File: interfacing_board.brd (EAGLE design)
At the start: 85.1 x 77.1 mm, 67 parts, among them IC1 MAX3096CSE, IC2 MAX3096CSE, X1 87758-3816, X2 87758-3816

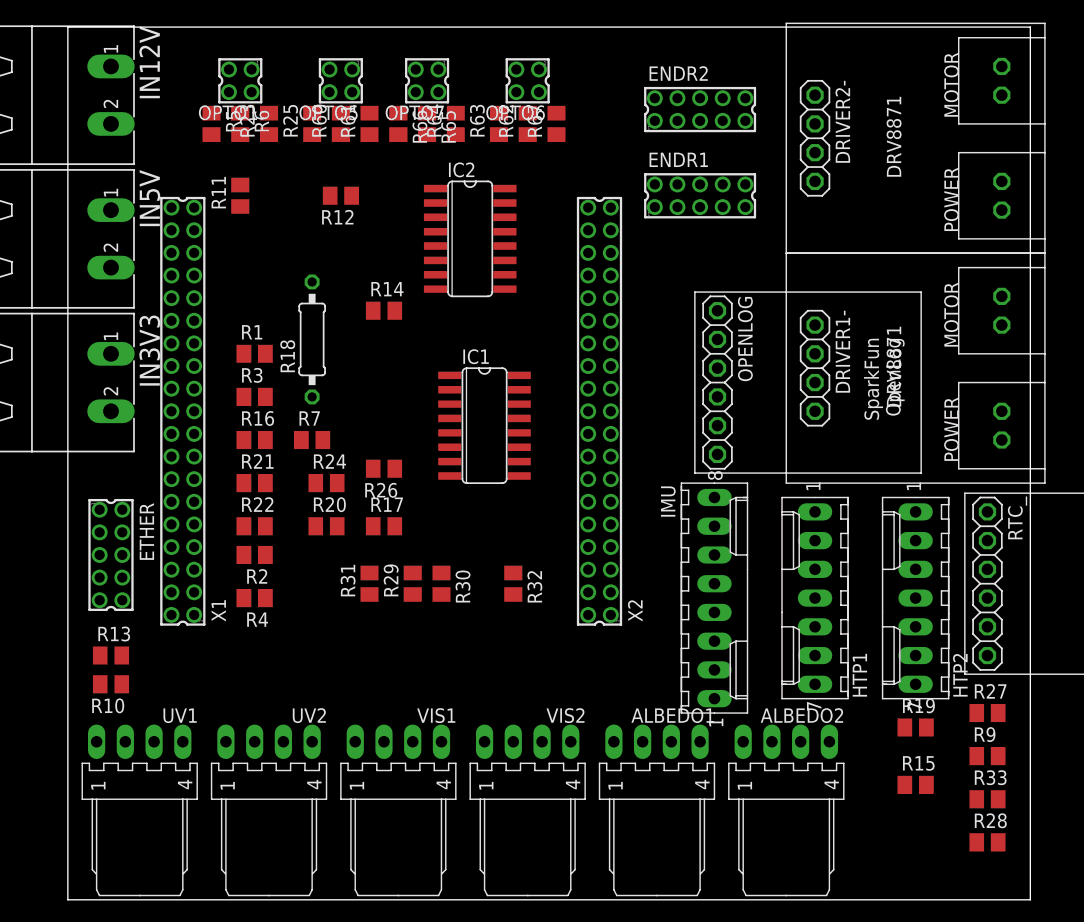
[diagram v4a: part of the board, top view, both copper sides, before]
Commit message: Autorouter on BIPOP board.
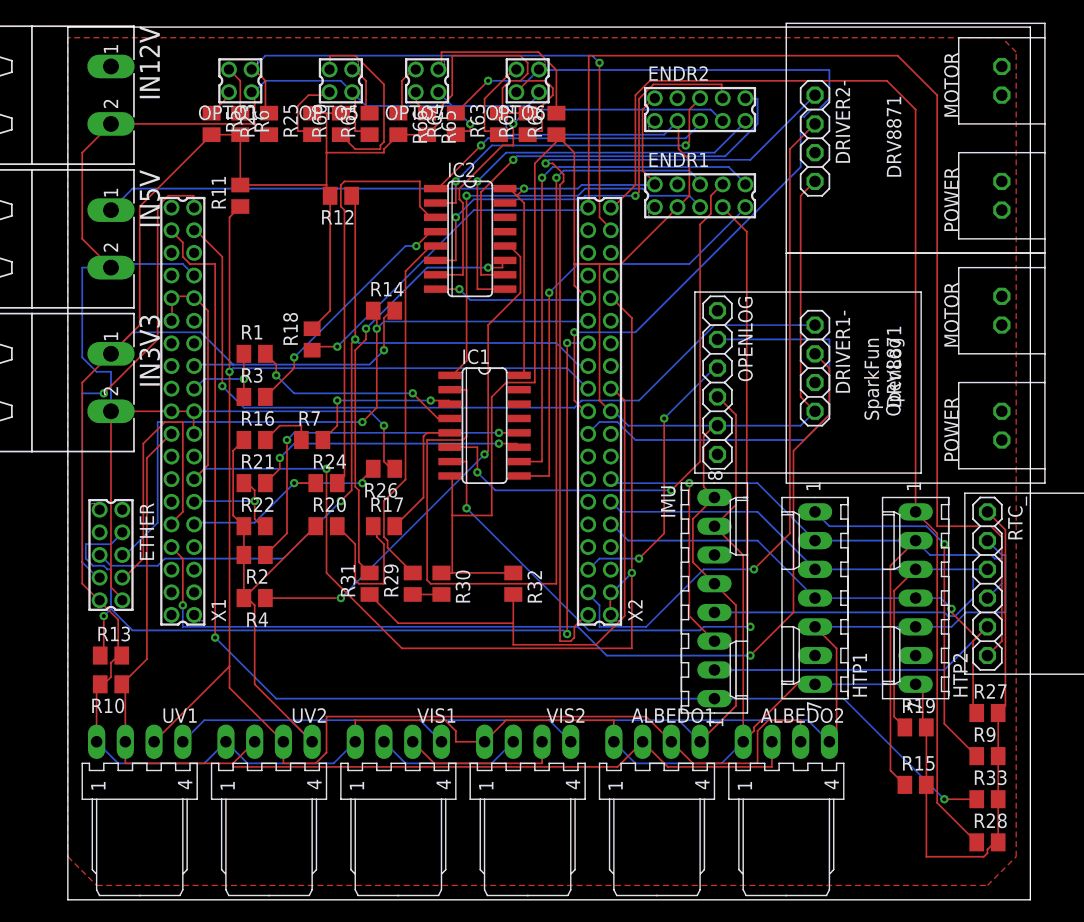
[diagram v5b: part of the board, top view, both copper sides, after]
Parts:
- R18: value 2k -> 4.7k; device eagle-ltspice:0207/10 -> rcl:R0805
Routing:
- net GND: track 0.00 -> 499.2 mm, vias 0 -> 3
- net 3.3V: track 0.00 -> 337.0 mm, vias 0 -> 1
- net SCL1: track 0.00 -> 149.7 mm, vias 0 -> 1
- net CS_RTC: track 0.00 -> 130.7 mm, vias 0 -> 1
- net CS_IMU: track 0.00 -> 112.1 mm, vias 0 -> 2
- net NC: track 0.00 -> 108.7 mm, vias 0 -> 2
- net CS_HTP2: track 0.00 -> 104.3 mm
- net SDA1: track 0.00 -> 95.3 mm
- net M11: track 0.00 -> 88.8 mm, vias 0 -> 2
- net SPI1_MISO: track 0.00 -> 84.6 mm, vias 0 -> 3
- net INCHA-1: track 0.00 -> 82.7 mm, vias 0 -> 1
- net SPI2_MOSI: track 0.00 -> 79.4 mm, vias 0 -> 1
- net IND2: track 0.00 -> 78.5 mm, vias 0 -> 2
- net SPI2_MISO: track 0.00 -> 77.1 mm
- net 5V: track 0.00 -> 76.1 mm, vias 0 -> 1
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- added copper zone on layer 1, net GND

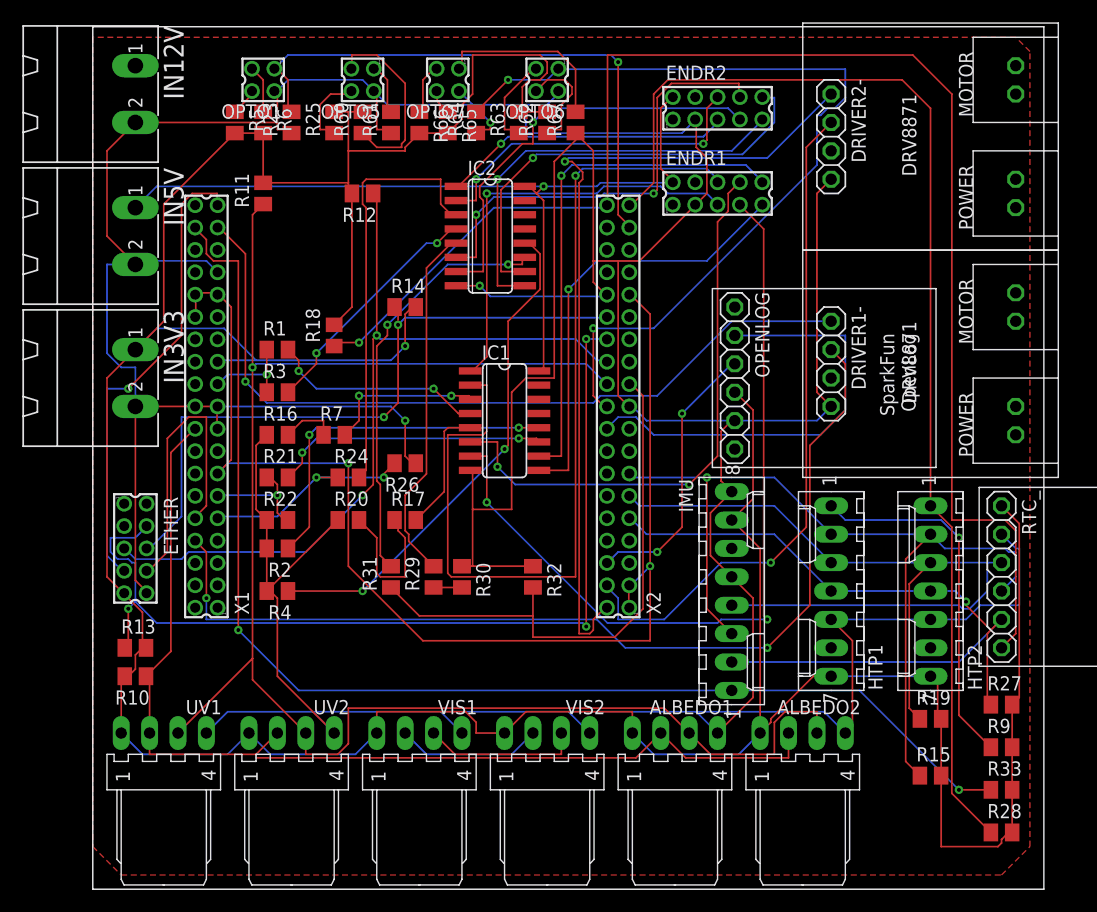
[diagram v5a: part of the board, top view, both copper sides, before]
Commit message: Changed connector in bipop_power_supply board, modified routing and board's dimensions.
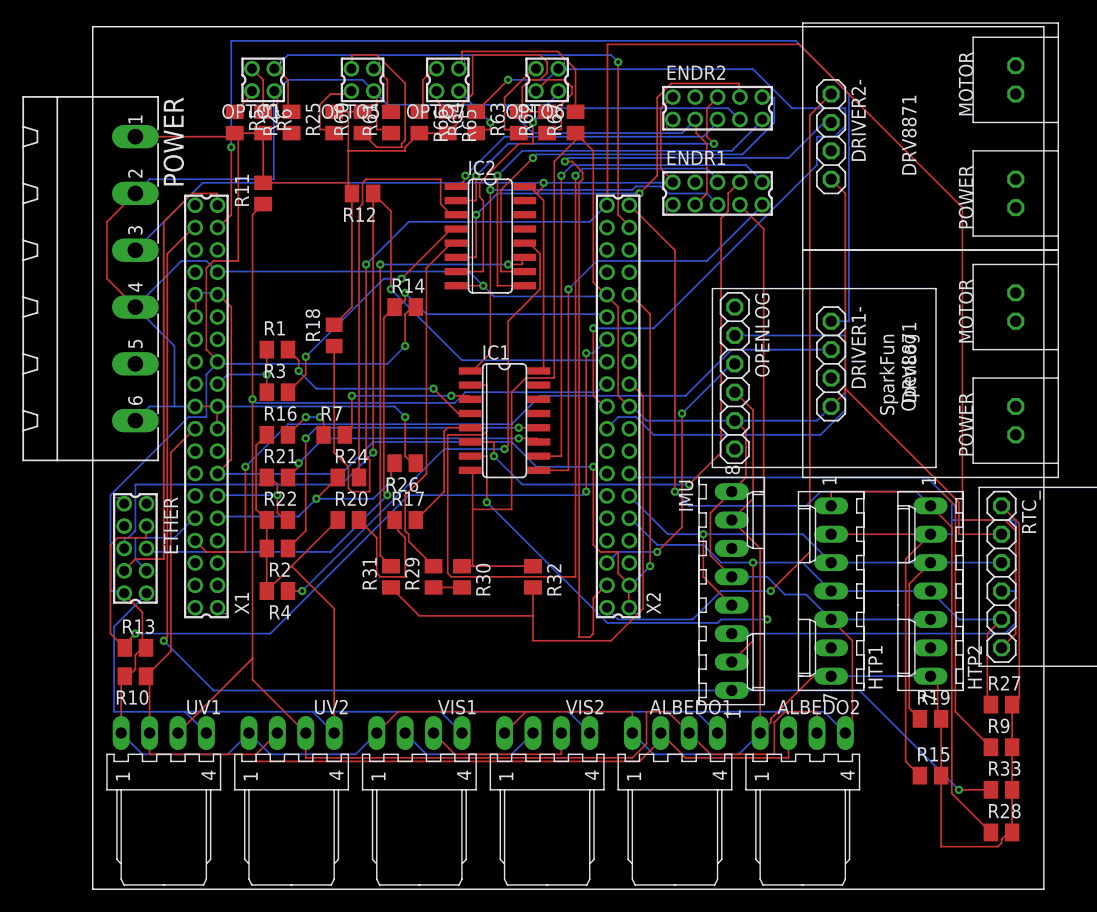
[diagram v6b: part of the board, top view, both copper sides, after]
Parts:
- removed IN12V, IN3V3, IN5V: MSTBA2, con-phoenix-508:MSTBA2
- added POWER: MSTBA6, con-phoenix-508:MSTBA6
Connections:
- net 12V: now also POWER.5; no longer IN12V.1
- net 3.3V: now also POWER.1; no longer IN3V3.1
- net 5V: now also POWER.3; no longer IN5V.1
- net GND: now also POWER.2, POWER.4, POWER.6; no longer IN12V.2, IN3V3.2, IN5V.2
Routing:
- net SPI2_MOSI: track 79.4 -> 108.6 mm, vias 1 -> 0
- net M12: track 71.1 -> 96.4 mm
- net CS_RTC: track 130.7 -> 155.7 mm
- net CS_HTP2: track 104.3 -> 83.2 mm, vias 0 -> 1
- net M11: track 88.8 -> 69.3 mm, vias 2 -> 1
- net SPI2_MISO: track 77.1 -> 58.3 mm, vias 0 -> 1
- net GND: track 499.2 -> 517.2 mm
- net ETH_RES: track 26.4 -> 9.41 mm
- net SPI2_SCK: track 70.6 -> 55.0 mm
- net M21: track 60.8 -> 75.2 mm
- net M22: track 73.7 -> 62.8 mm
- net SPI1_MOSI: track 73.3 -> 83.2 mm
- net NC: track 108.7 -> 99.5 mm
- net SPI1_MISO: track 84.6 -> 76.4 mm
- net CS_IMU: track 112.1 -> 117.7 mm
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- removed copper zone on layer 1, net GND

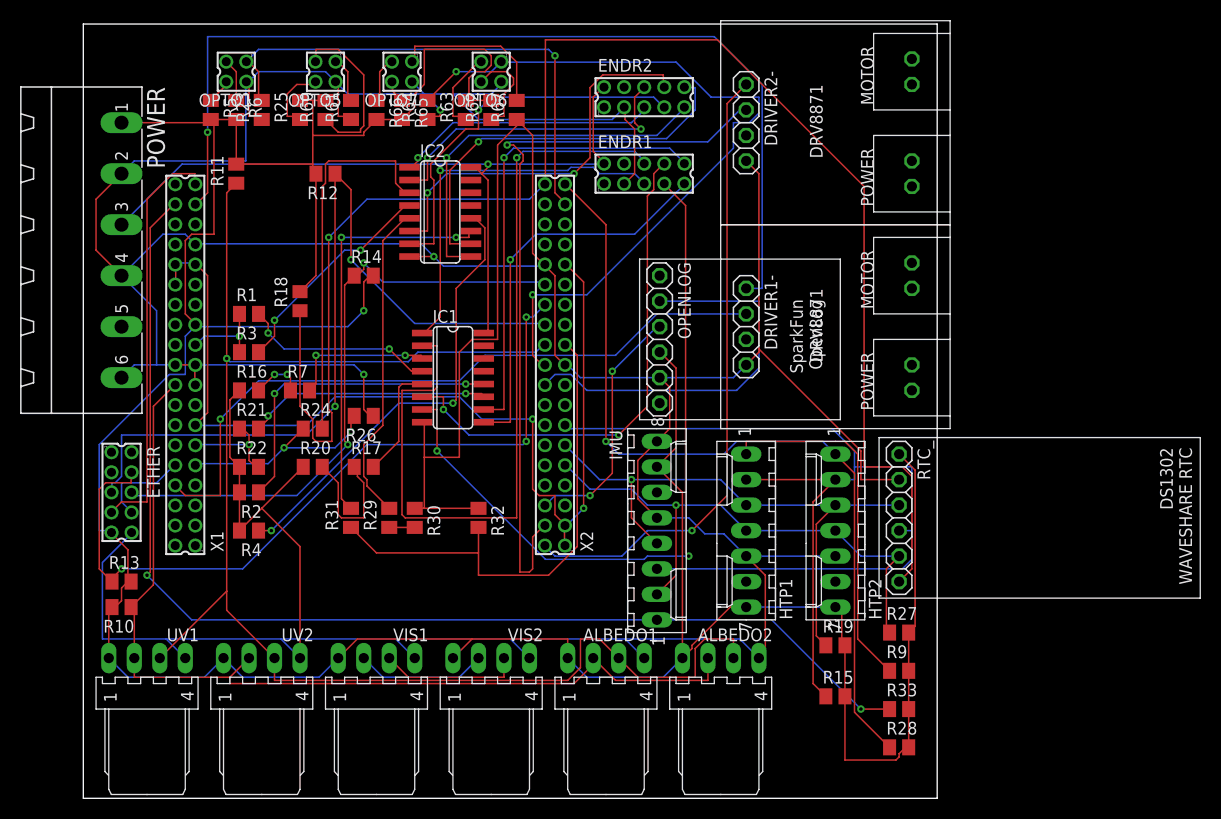
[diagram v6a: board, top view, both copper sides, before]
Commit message: Circuit converted to single-periscope operation mode. Duplicate components removed.
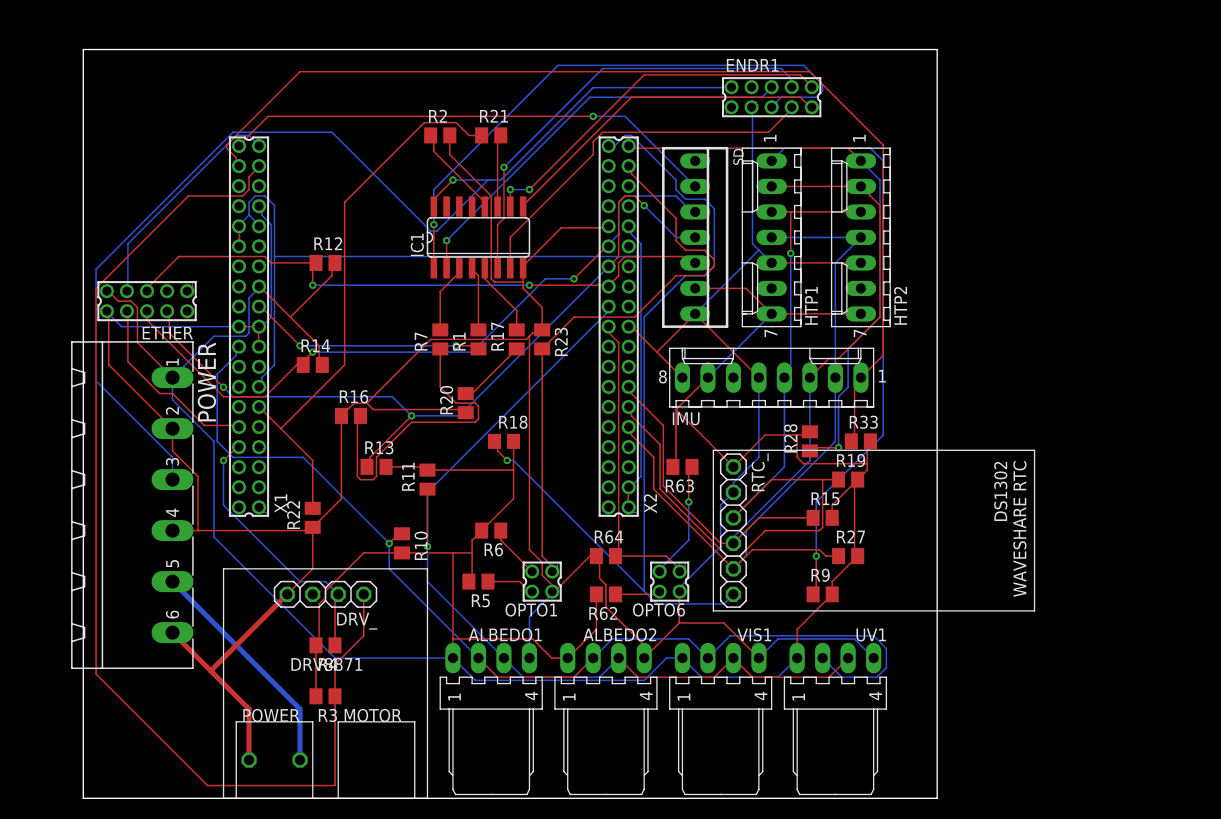
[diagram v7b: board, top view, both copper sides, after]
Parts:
- removed DRIVER1-, DRIVER2-: DRV8871, SKA_EP_molex_6410_7395:1X06
- removed ENDR2: 332-10, con-garry:332-10
- removed IC2: MAX3096CSE, maxim:SO16
- removed OPENLOG: OPENLOG, SKA_EP_molex_6410_7395:OPENLOG
- removed OPTO5, OPTO7: 332-04, con-garry:332-04
- removed R24, R29, R31: 5k, rcl:M0805
- removed R25, R60, R61, R65, R66, R67: (no value), resistor:M0805
- removed R26, R30, R32: 10k, rcl:M0805
- removed UV2, VIS2: 22-05-7048-04, EP_molex_6410_7395:7395-04
- added DRV_: DRV8871, customy:DRIVER
- added SD: 22-23-2071, con-molex:22-23-2071
- moved UV1 68.6 mm to (74.9, 36.8)
- moved OPTO1 59.2 mm to (45.7, 44.5)
- moved R5 54.0 mm to (39.4, 44.5), turned to 180 degrees
- moved OPTO6 53.8 mm to (58.4, 44.5)
- moved R62 49.6 mm to (52.1, 43.2), turned to 180 degrees
- moved R6 49.0 mm to (40.6, 49.5), turned to 180 degrees
- moved R64 47.9 mm to (52.1, 47.0), turned to 0 degrees
- moved R63 41.6 mm to (59.7, 55.9), turned to 180 degrees
- moved R2 40.3 mm to (35.6, 88.9), turned to 0 degrees
- moved R21 37.9 mm to (40.6, 88.9)
- moved R23 36.1 mm to (45.7, 68.6), turned to 270 degrees
- moved R11 35.9 mm to (34.3, 54.6)
- moved R3 35.1 mm to (24.1, 33.0), turned to 180 degrees
- moved VIS1 34.3 mm to (63.5, 36.8)
- moved R28 31.8 mm to (72.4, 58.4), turned to 90 degrees
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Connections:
- removed net CHA-2: IC2.3, R24.2
- removed net CHB-2: IC2.5, R29.2
- removed net CHB2-L: R29.1, R30.2
- removed net CHC-2: IC2.11, R31.2
- removed net DRV2-VM: DRIVER2-.VM
- removed net INCHA-2: ENDR2.6, IC2.2
- removed net INCHB-2: ENDR2.8, IC2.6
- removed net INCHC-2: ENDR2.10, IC2.10
- removed net IND3: OPTO5.1, R61.2
- removed net IND4: OPTO7.1, R67.2
- removed net N$11: OPTO5.4, R25.1
- removed net N$13: IC2.12, R4.1
- removed net N$16: OPTO7.3, R66.1
- removed net N$23: OPTO7.4, R65.1
- removed net N$5: OPTO5.3, R60.1
- removed net N$8: IC2.4, R3.2
- removed net OL-BLK: OPENLOG.OLBLK
- removed net OL-GRN: OPENLOG.OLGRN
- removed net SCL2: VIS1.3, VIS2.3
- removed net SDA2: VIS1.2, VIS2.2
- removed net ~INCHA-2: ENDR2.5, IC2.1
- removed net ~INCHB-2: ENDR2.7, IC2.7
- removed net ~INCHC-2: ENDR2.9, IC2.9
- new net CD_SD: SD.1
- net +5V: no longer R3.1
- net 12V: now also DRV_.MOTOR_VCC
- net 3.3V: now also R3.2, R4.2, SD.6; no longer OPENLOG.OLVCC, R25.2, R60.2, R65.2, R66.2, UV2.1, VIS2.1
- net 5V: no longer ENDR2.2, IC2.16
- net CHA-2L: no longer R24.1, R26.2
- net CHC-2L: no longer R31.1, R32.2
- net CS_SD: now also SD.2
- net DRV1-VM: now also DRV_.VM; no longer DRIVER1-.VM
- net GND: now also DRV_.GND, DRV_.MOTOR_GND, SD.7; no longer DRIVER1-.GND, DRIVER2-.GND, ENDR2.3, IC2.8, OPENLOG.OLGND, OPTO5.2, OPTO7.2, R26.1, R30.1, R32.1, R4.2, R61.1, R67.1, UV2.4, VIS2.4
- net M11: now also DRV_.IN1, R4.1; no longer DRIVER1-.IN1
- net M12: now also DRV_.IN2, R3.1; no longer DRIVER1-.IN2
- net M21: no longer DRIVER2-.IN1
- net M22: no longer DRIVER2-.IN2
- net OL_RX: no longer OPENLOG.OLRXI
- net OL_TX: no longer OPENLOG.OLTXO
- net SCL1: now also VIS1.3; no longer UV2.3
- net SDA1: now also VIS1.2; no longer UV2.2
- net SPI1_MISO: now also SD.4
- net SPI1_MOSI: now also SD.5
- net SPI1_SCK: now also SD.3
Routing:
- net GND: track 517.2 -> 350.9 mm, vias 3 -> 0
- net M21: track 75.2 -> 0.00 mm, vias 1 -> 0
- net CS_RTC: track 155.7 -> 88.1 mm
- net M22: track 62.8 -> 0.00 mm, vias 1 -> 0
- net SCL1: track 149.7 -> 90.5 mm
- net CHC-2L: track 50.2 -> 0.00 mm
- net CS_SD: track 0.00 -> 49.6 mm, vias 0 -> 1
- net IND2: track 76.8 -> 30.5 mm, vias 2 -> 0
- net N$13: track 45.2 -> 0.00 mm, vias 2 -> 0
- net CHC-1L: track 10.3 -> 55.0 mm, vias 1 -> 0
- net M11: track 69.3 -> 26.8 mm
- net INCHA-1: track 82.7 -> 41.5 mm
- net CHC-2: track 40.9 -> 0.00 mm, vias 2 -> 0
- net OL_RX: track 39.9 -> 0.00 mm
- net INCHC-2: track 39.7 -> 0.00 mm, vias 1 -> 0
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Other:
- board size 85.1 x 77.1 mm -> 85.1 x 74.6 mm
